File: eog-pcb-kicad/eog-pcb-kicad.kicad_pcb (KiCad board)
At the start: 4 copper layers, 92 x 60 mm, 103 parts, among them J1 Conn_01x03, J2 Conn_01x02, J3 Conn_01x02, J4 Conn_01x03, J6 Conn_01x02, U2 AD620, U3 LMC6482, U4 LMC6482, U5 AD620, U6 LMC6482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

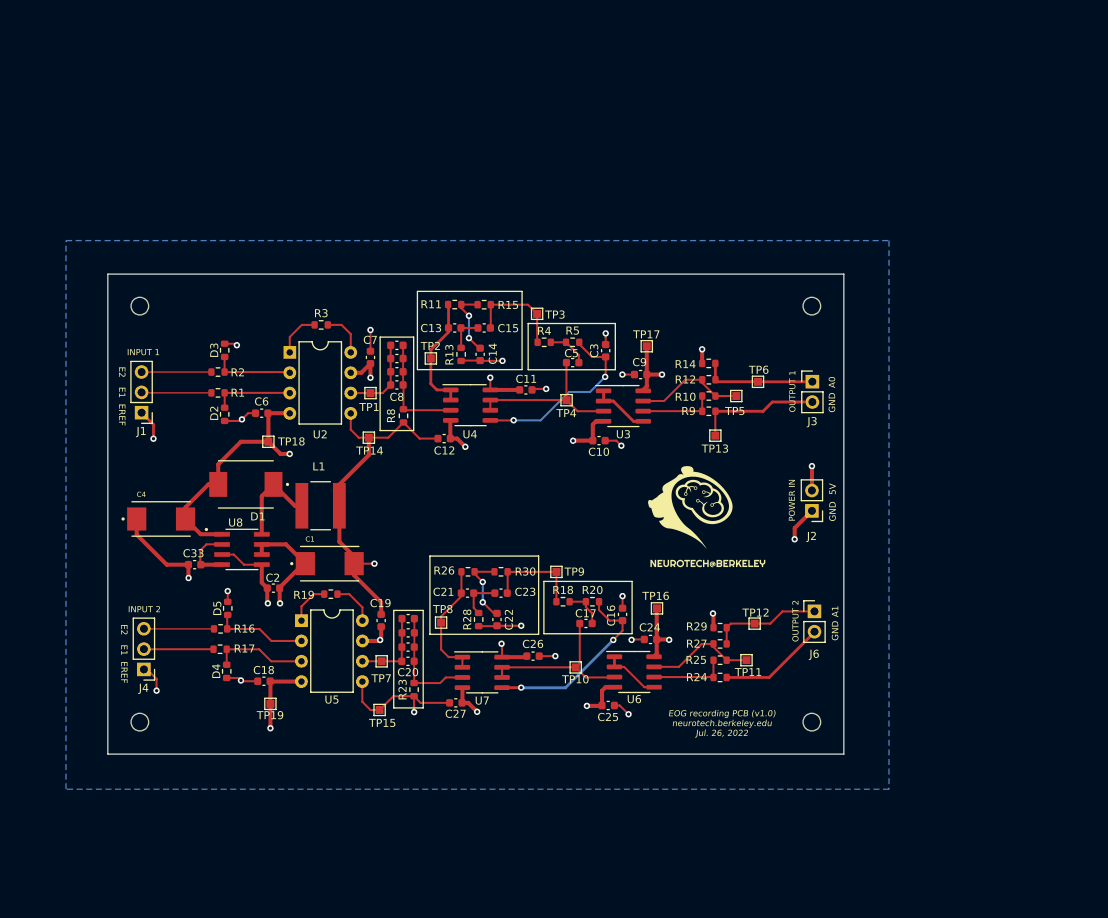
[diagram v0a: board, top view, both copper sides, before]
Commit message: added libraries for digipots and started reorganizing the pcb for 2nd version
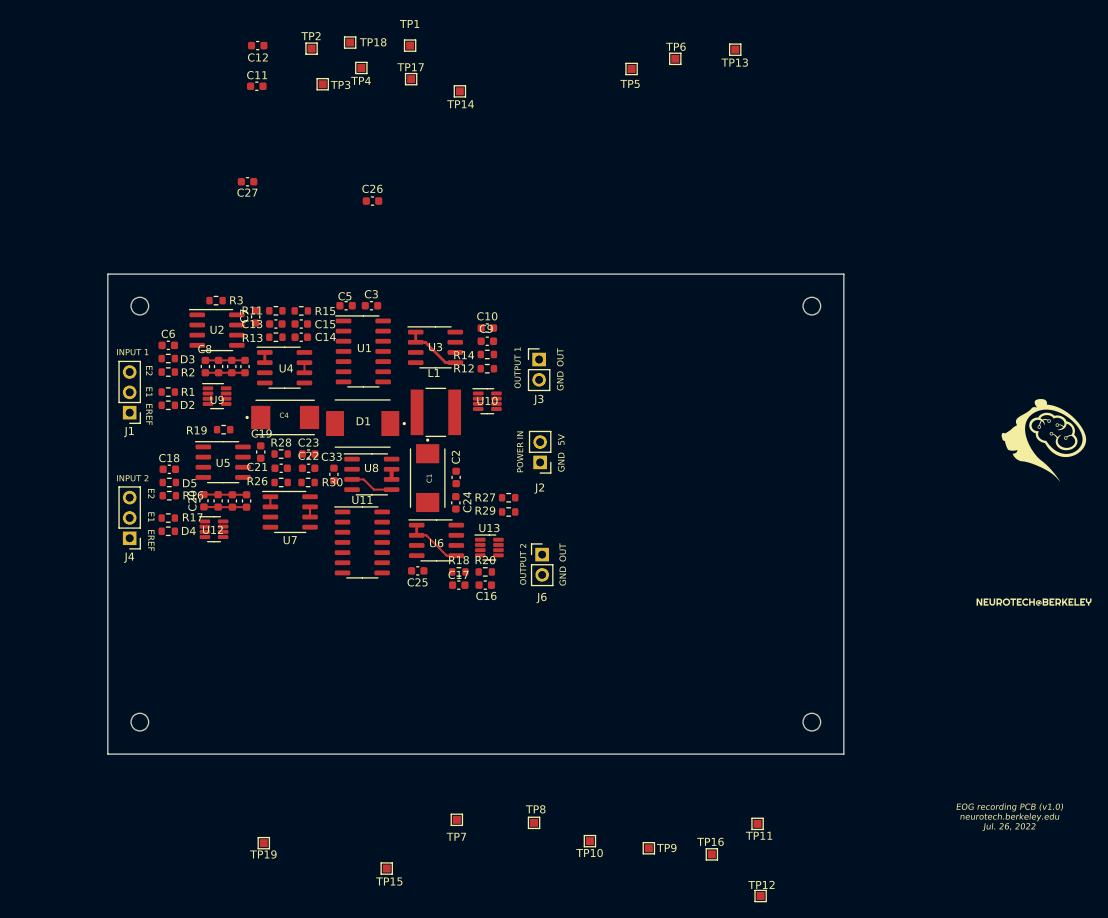
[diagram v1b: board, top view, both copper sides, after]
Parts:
- removed R10, R25: 100k, Resistor_SMD:R_0603_1608Metric
- removed R23, R8: 10k, Resistor_SMD:R_0603_1608Metric
- removed R24, R9: 150R, Resistor_SMD:R_0603_1608Metric
- removed R4, R5: 320R, Resistor_SMD:R_0603_1608Metric
- added U1: AD8402ARZ1, Package_SO:SOIC-14_3.9x8.7mm_P1.27mm, F.Cu at (128.0, 74.5)
- added U10: MAX5401EKAT, Package_TO_SOT_SMD:SOT-23-8, F.Cu at (143.5, 80.8)
- added U11: AD8402ARZ1, Package_SO:SOIC-14_3.9x8.7mm_P1.27mm, F.Cu at (127.9, 98.4)
- added U12: AD5160BRJZ5-RL7, Package_TO_SOT_SMD:SOT-23-8, F.Cu at (109.3, 96.8)
- added U13: MAX5401EKAT, Package_TO_SOT_SMD:SOT-23-8, F.Cu at (143.8, 99.1)
- added U9: AD5160BRJZ5-RL7, Package_TO_SOT_SMD:SOT-23-8, F.Cu at (109.7, 80.1)
- U2, U5: footprint Package_DIP:DIP-8_W7.62mm -> Package_SO:SOIC-8_3.9x4.9mm_P1.27mm
- U8: footprint MAX764ESA_:SOIC127P600X175-8N -> Package_SO:SOIC-8_3.9x4.9mm_P1.27mm
- moved C27 70.1 mm to (113.5, 53.3)
- moved C26 60.3 mm to (129.2, 55.8)
- moved C12 54.4 mm to (114.8, 36.3)
- moved TP18 50.9 mm to (126.4, 35.9)
- moved C11 50.7 mm to (114.7, 41.4)
- moved TP4 48.8 mm to (127.8, 39.1)
- moved TP13 48.3 mm to (174.5, 36.8)
- moved G*** 45.0 mm to (213.4, 85.7)
- moved TP14 44.8 mm to (140.1, 42.0)
- moved TP17 44.5 mm to (134.0, 40.5)
- moved TP1 43.7 mm to (133.9, 36.3)
- moved TP5 42.9 mm to (161.5, 39.2)
- moved TP6 41.7 mm to (167.0, 38.0)
- moved TP2 41.5 mm to (121.5, 36.7)
- moved ? 41.1 mm to (211.8, 105.9)
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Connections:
- net /LPF_OUT_CH0 renamed /LPF_IN-_CH0
- net /LPF_OUT_CH1 renamed /LPF_IN-_CH1
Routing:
- net GND: track 162.2 -> 5.54 mm, vias 22 -> 0
- net VDD_NEG_5V: track 61.5 -> 0.00 mm, vias 6 -> 0
- net VDD: track 55.0 -> 1.27 mm, vias 10 -> 0
- net /LPF_IN+_CH1: track 23.8 -> 0.00 mm, vias 2 -> 0
- net /LPF_IN+_CH0: track 23.3 -> 0.00 mm, vias 2 -> 0
- net /LPF_IN-_CH1: track 21.6 -> 1.34 mm
- net /LPF_IN-_CH0: track 20.7 -> 1.29 mm
- net /AOUT_CH0: track 14.0 -> 0.00 mm
- net /AOUT_CH1: track 13.9 -> 0.01 mm
- net /NOTCH_IN_CH1: track 15.1 -> 1.27 mm
- net /AMP_OUT_CH1: track 13.8 -> 0.00 mm
- net /AMP_OUT_CH0: track 13.8 -> 0.00 mm
- net /NOTCH_IN_CH0: track 14.6 -> 1.27 mm
- net NOTCH_OUT_CH0: track 12.7 -> 0.00 mm
- net NOTCH_OUT_CH1: track 12.5 -> 0.00 mm
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- removed copper zone on B.Cu, net VDD_NEG_5V
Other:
- board text added: "OUT"
- board text removed: "A0"
- board text removed: "A1"

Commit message: progress on layout
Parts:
- removed J3, J6: Conn_01x02, Connector_PinHeader_2.54mm:PinHeader_1x02_P2.54mm_Vertical
- removed R18, R20: 320R, Resistor_SMD:R_0603_1608Metric
- removed TP12, TP6: TestPoint, TestPoint:TestPoint_Pad_1.0x1.0mm
- added R24: 150R, Resistor_SMD:R_0603_1608Metric, F.Cu at (145.0, 95.4)
- added R4: 150, Resistor_SMD:R_0603_1608Metric, F.Cu at (143.9, 73.0)
- J2: value Conn_01x02 -> Conn_01x12; footprint Connector_PinHeader_2.54mm:PinHeader_1x02_P2.54mm_Vertical -> Connector_PinHeader_2.54mm:PinHeader_1x12_P2.54mm_Vertical
- moved C27 57.3 mm to (119.2, 110.4)
- moved C26 45.8 mm to (120.7, 100.7)
- moved H3 38.2 mm to (148.6, 106.8)
- moved H2 34.7 mm to (149.4, 68.5)
- moved C11 33.6 mm to (123.6, 73.8), turned to 90 degrees
- moved C2 15.6 mm to (155.2, 90.8), turned to 180 degrees
- moved H4 14.1 mm to (99.6, 106.8)
- moved J2 13.3 mm to (150.4, 101.7)
- moved U8 12.3 mm to (120.0, 81.7)
- moved C1 12.2 mm to (145.7, 82.9)
- moved R27 10.6 mm to (136.0, 95.7), turned to 90 degrees
- moved C10 10.5 mm to (133.6, 75.2), turned to 90 degrees
- moved C16 10.1 mm to (143.9, 113.8)
- moved C17 10.1 mm to (140.6, 113.8)
- moved C33 9.62 mm to (114.9, 87.9)
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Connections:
- C17 pad 1: Net-(C17-Pad1) -> Net-(U11-Pad14)
- J2 pad 2: VDD -> AOUT_CH1
- R12 pad 1: /AOUT_CH0 -> AOUT_CH0
- R12 pad 2: /AMP_OUT_CH0 -> Net-(U10-Pad1)
- R14 pad 1: /AOUT_CH0 -> AOUT_CH0
- R27 pad 1: /AOUT_CH1 -> AOUT_CH1
- R29 pad 1: /AOUT_CH1 -> AOUT_CH1
- TP5 pad 1: /AMP_OUT_CH0 -> Net-(U10-Pad1)
- U1 pad 1: unconnected-(U1-Pad1) -> GND
- U1 pad 11: unconnected-(U1-Pad11) -> VDD
- U1 pad 12: unconnected-(U1-Pad12) -> NOTCH_OUT_CH0
- U1 pad 13: unconnected-(U1-Pad13) -> NOTCH_OUT_CH0
- U1 pad 14: unconnected-(U1-Pad14) -> Net-(C5-Pad1)
- U1 pad 2: unconnected-(U1-Pad2) -> /LPF_IN+_CH0
- U1 pad 3: unconnected-(U1-Pad3) -> Net-(C5-Pad1)
- U1 pad 4: unconnected-(U1-Pad4) -> Net-(C5-Pad1)
- U1 pad 5: unconnected-(U1-Pad5) -> GND
- U1 pad 7: unconnected-(U1-Pad7) -> CS3
- U1 pad 8: unconnected-(U1-Pad8) -> SDI
- U1 pad 9: unconnected-(U1-Pad9) -> CLK
- U10 pad 1: unconnected-(U10-Pad1) -> Net-(U10-Pad1)
- U10 pad 2: unconnected-(U10-Pad2) -> GND
- U10 pad 3: unconnected-(U10-Pad3) -> CS5
- U10 pad 4: unconnected-(U10-Pad4) -> SDI
- U10 pad 5: unconnected-(U10-Pad5) -> CLK
- U10 pad 6: unconnected-(U10-Pad6) -> VDD
- U10 pad 7: unconnected-(U10-Pad7) -> /AMP_IN-_CH0
- U10 pad 8: unconnected-(U10-Pad8) -> /AMP_IN-_CH0
- U11 pad 1: unconnected-(U11-Pad1) -> GND
- U11 pad 11: unconnected-(U11-Pad11) -> VDD
- U11 pad 12: unconnected-(U11-Pad12) -> NOTCH_OUT_CH1
- U11 pad 13: unconnected-(U11-Pad13) -> NOTCH_OUT_CH1
- U11 pad 14: unconnected-(U11-Pad14) -> Net-(U11-Pad14)
- U11 pad 2: unconnected-(U11-Pad2) -> /LPF_IN+_CH1
- U11 pad 3: unconnected-(U11-Pad3) -> Net-(U11-Pad14)
- U11 pad 4: unconnected-(U11-Pad4) -> Net-(U11-Pad14)
- U11 pad 5: unconnected-(U11-Pad5) -> GND
- U11 pad 7: unconnected-(U11-Pad7) -> CS4
- U11 pad 8: unconnected-(U11-Pad8) -> SDI
- U11 pad 9: unconnected-(U11-Pad9) -> CLK
- U12 pad 4: unconnected-(U12-Pad4) -> CLK
- U12 pad 5: unconnected-(U12-Pad5) -> SDI
- U12 pad 6: unconnected-(U12-Pad6) -> CS2
- U12 pad 8: VDD -> /HPF_OUT_CH1
- U13 pad 1: unconnected-(U13-Pad1) -> /AMP_OUT_CH1
- U13 pad 2: unconnected-(U13-Pad2) -> GND
- U13 pad 3: unconnected-(U13-Pad3) -> CS6
- U13 pad 4: unconnected-(U13-Pad4) -> SDI
- U13 pad 5: unconnected-(U13-Pad5) -> CLK
- U13 pad 6: unconnected-(U13-Pad6) -> VDD
- U13 pad 7: unconnected-(U13-Pad7) -> /AMP_IN-_CH1
- U13 pad 8: unconnected-(U13-Pad8) -> /AMP_IN-_CH1
- U3 pad 7: /AMP_OUT_CH0 -> Net-(U10-Pad1)
- U9 pad 4: unconnected-(U9-Pad4) -> CLK
- U9 pad 5: unconnected-(U9-Pad5) -> SDI
- U9 pad 6: unconnected-(U9-Pad6) -> CS1
- U9 pad 8: VDD -> /HPF_OUT_CH0
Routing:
- net NOTCH_OUT_CH0: track 0.00 -> 22.3 mm
- net /LPF_IN-_CH0: track 1.29 -> 17.5 mm, vias 0 -> 2
- net AOUT_CH0: track 0.00 -> 16.1 mm, vias 0 -> 2
- net /LPF_IN+_CH0: track 0.00 -> 14.8 mm
- net /HPF_OUT_CH0: track 5.02 -> 15.4 mm
- net Net-(U10-Pad1): track 0.00 -> 10.0 mm, vias 0 -> 2
- net /AMP_IN-_CH0: track 0.00 -> 9.78 mm
- net GND: track 5.54 -> 14.3 mm, vias 0 -> 2
- net Net-(C5-Pad1): track 0.00 -> 7.27 mm
- net NOTCH_OUT_CH1: track 0.00 -> 7.17 mm
- net VDD: track 1.27 -> 7.54 mm
- net /IA_OUT_CH0: track 4.95 -> 10.8 mm
- net /HPF_OUT_CH1: track 5.34 -> 10.7 mm
- net /IA_OUT_CH1: track 5.34 -> 10.5 mm
- net /NOTCH_IN_CH0: track 1.27 -> 4.87 mm
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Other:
- board size 92 x 60 mm -> 58.2 x 43.6 mm
- board text removed: "5V"
- board text removed: "GND"
- board text removed: "OUT"
- board text removed: "OUTPUT 1"
- board text removed: "OUTPUT 2"
- board text removed: "POWER IN"
